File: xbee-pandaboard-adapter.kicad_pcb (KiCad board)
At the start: 2 copper layers, 29.5 x 42.7 mm, 19 parts, among them IC1 MCP1700, Q1 2N7000

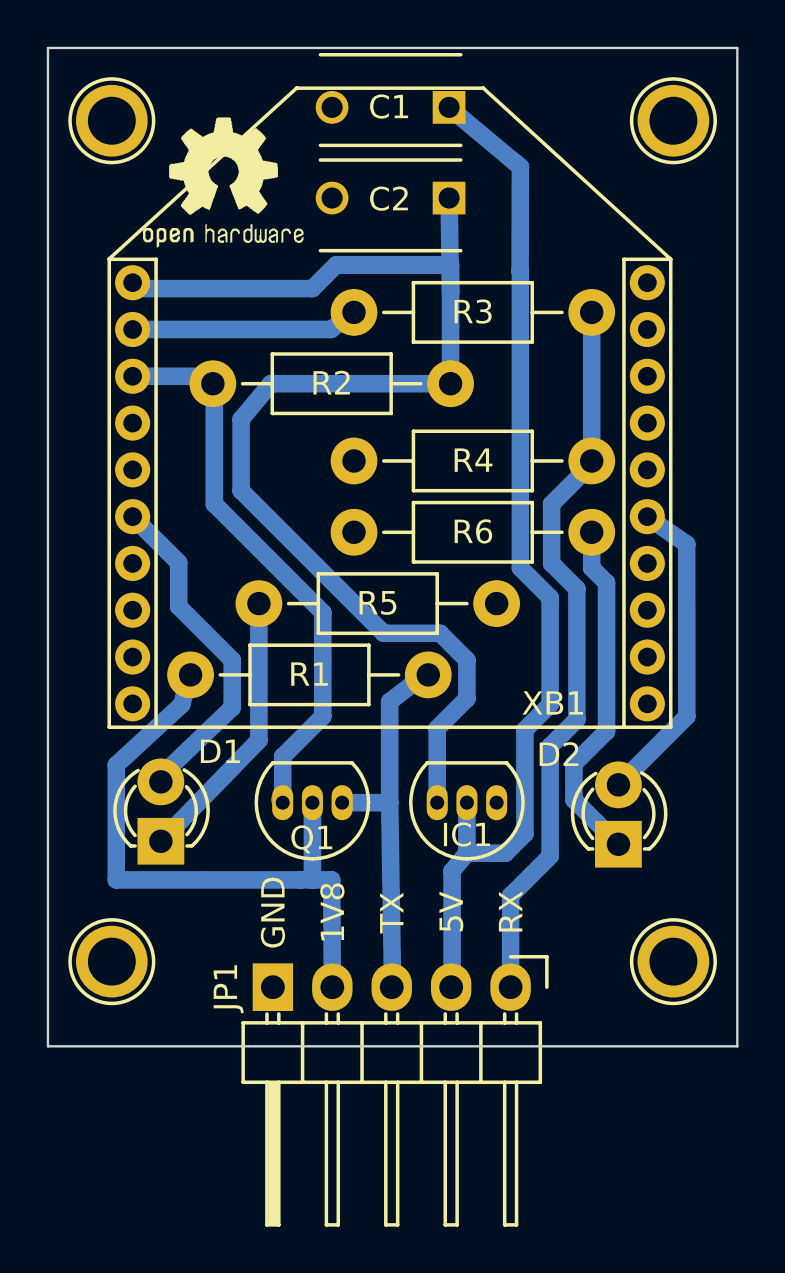
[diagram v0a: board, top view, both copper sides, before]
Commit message: Increased trace clearance and spoke width.
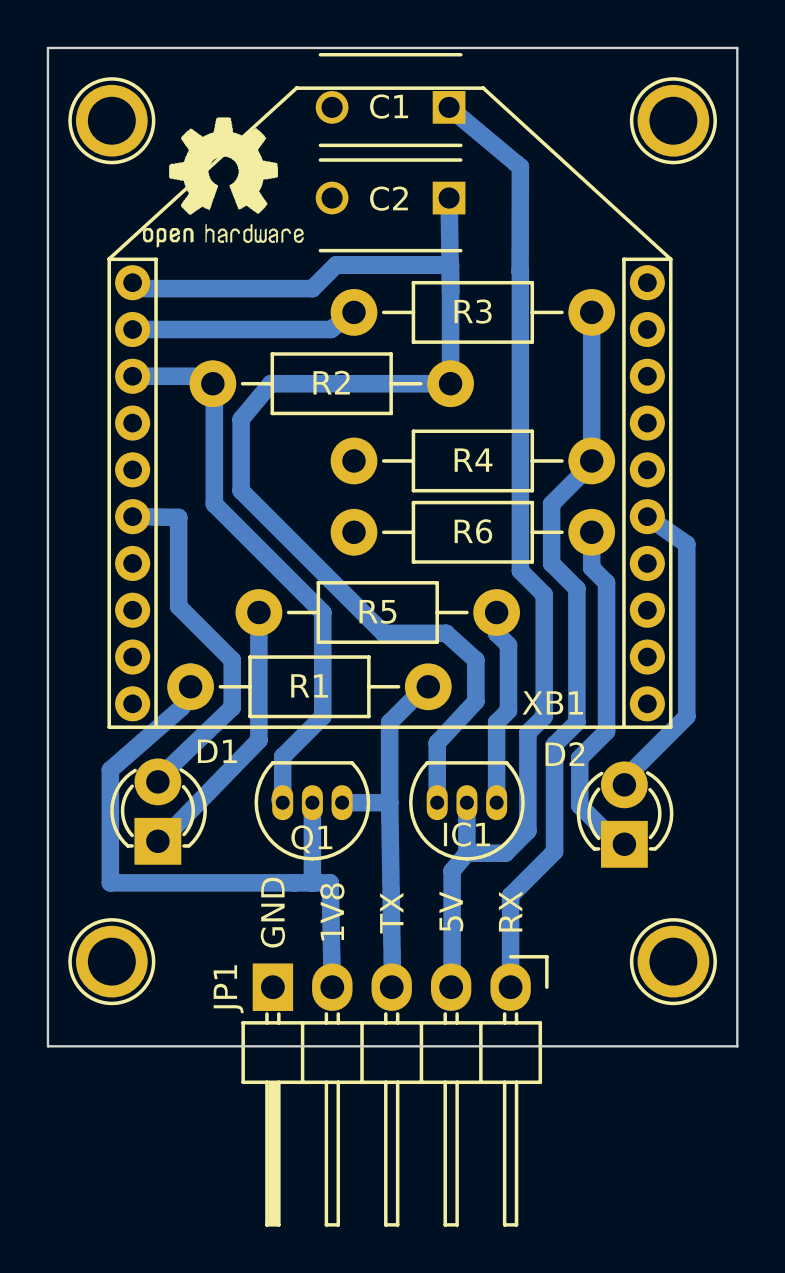
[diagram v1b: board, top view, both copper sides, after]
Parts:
- moved R1 0.51 mm to (140.6, 103.4)
- moved R5 0.38 mm to (143.5, 100.2)
- moved D2 0.25 mm to (159.1, 110.1)
- moved D1 0.13 mm to (139.2, 110.0)
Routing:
- net GNDREF: track 0.00 -> 8.55 mm
- net Net-(D1-Pad2): track 14.4 -> 15.5 mm
- net UART_TX: track 16.3 -> 15.5 mm
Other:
- net class Default: clearance 0.2 -> 0.3
- rule trace_clearance: 0.2 -> 0.3
